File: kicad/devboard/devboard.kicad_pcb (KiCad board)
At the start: 2 copper layers, 34.5 x 25 mm, 37 parts, among them J1 USB_C_Receptacle, J2 Conn_02x02_Top_Bottom, J3 Conn_01x04_Socket, Q1 BSS138, U1 LM3940, U2 CH340G, U3 STM32G030K8Tx, Y1 12 MHz, Y2 8 MHz

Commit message: niche GND prettying up
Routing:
- net GND: track 19.8 -> 14.4 mm
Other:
- board text added: "Boot"
- board text added: "Breakout v1"
- board text added: "Reset"

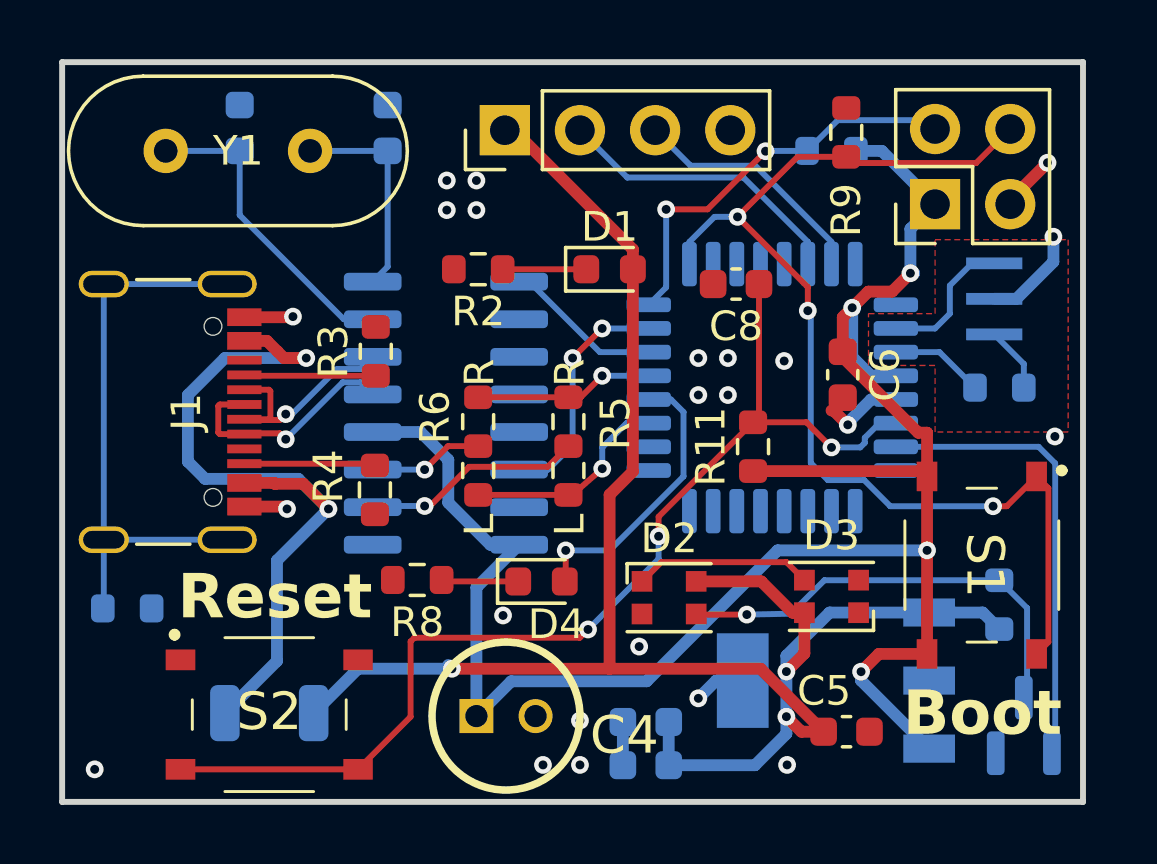
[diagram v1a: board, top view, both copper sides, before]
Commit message: Added silkscreen labels
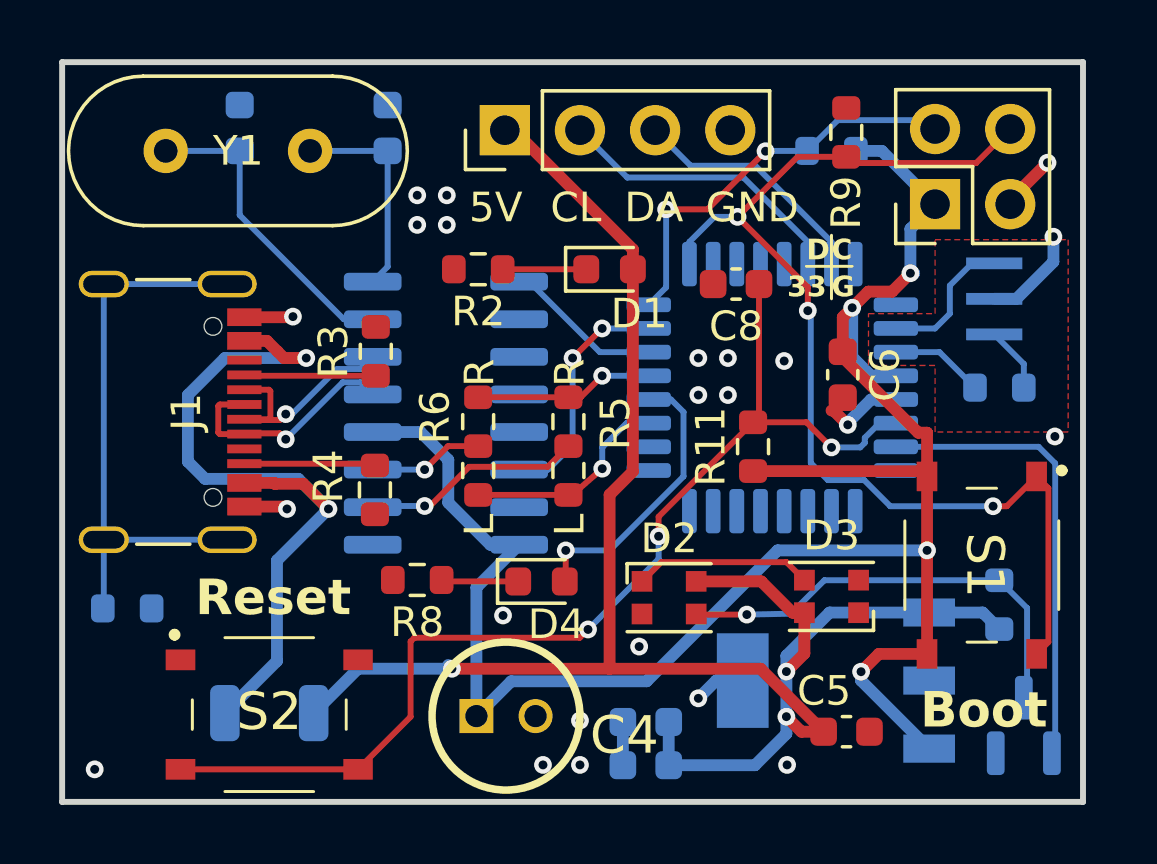
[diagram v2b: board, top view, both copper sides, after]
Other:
- board text added: "33"
- board text added: "5V"
- board text added: "C"
- board text added: "CL"
- board text added: "D"
- board text added: "DA"
- board text added: "G"
- board text added: "GND"
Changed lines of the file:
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@@
 		(tags "LED")
 		(property "Reference" "D1"
-			(at 0 -1.43 0)
+			(at 1 1.5 0)
 			(layer "F.SilkS")
 			(effects
@@
 		(tags "resistor")
 		(property "Reference" "R9"
-			(at -2.625 0 -90)
+			(at -2.375 0 -90)
 			(layer "F.SilkS")
 			(effects
@@
 		(layer "B.SilkS")
 	)
+	(gr_line
+		(start 126.15 55.9)
+		(end 127.7 55.9)
+		(stroke
+			(width 0.1)
+			(type default)
+		)
+		(layer "F.SilkS")
+	)
+	(gr_line
+		(start 127 54.85)
+		(end 127 57)
+		(stroke
+			(width 0.1)
+			(type default)
+		)
+		(layer "F.SilkS")
+	)
 	(gr_rect
 		(start 101 49)
@@
 		)
 	)
+	(gr_text "CL"
+		(at 117.5 54.5 0)
+		(layer "F.SilkS")
+		(effects
+			(font
+				(size 1 1)
+				(thickness 0.15)
+			)
+			(justify left bottom)
+		)
+	)
+	(gr_text "D"
+		(at 126.15 55.75 0)
+		(layer "F.SilkS")
+		(effects
+			(font
+				(size 0.7 0.7)
+				(thickness 0.15)
+				(bold yes)
+			)
+			(justify left bottom)
+		)
+	)
+	(gr_text "5V"
+		(at 114.75 54.5 0)
+		(layer "F.SilkS")
+		(effects
+			(font
+				(size 1 1)
+				(thickness 0.15)
+			)
+			(justify left bottom)
+		)
+	)
+	(gr_text "C"
+		(at 127 55.75 0)
+		(layer "F.SilkS")
+		(effects
+			(font
+				(size 0.7 0.7)
+				(thickness 0.15)
+				(bold yes)
+			)
+			(justify left bottom)
+		)
+	)
+	(gr_text "G"
+		(at 127 57 0)
+		(layer "F.SilkS")
+		(effects
+			(font
+				(size 0.7 0.7)
+				(thickness 0.15)
+				(bold yes)
+			)
+			(justify left bottom)
+		)
+	)
+	(gr_text "33"
+		(at 125.5 57 0)
+		(layer "F.SilkS")
+		(effects
+			(font
+				(size 0.7 0.7)
+				(thickness 0.15)
+				(bold yes)
+			)
+			(justify left bottom)
+		)
+	)
 	(gr_text "Reset"
-		(at 104.902 67.945 0)
+		(at 105.5 67.8 0)
 		(layer "F.SilkS")
 		(effects
 			(font
-				(size 1.5 1.5)
-				(thickness 0.3)
+				(size 1.2 1.2)
+				(thickness 0.25)
 				(bold yes)
 			)
@@
 	)
 	(gr_text "Boot"
-		(at 129.413 71.882 0)
+		(at 130 71.6 0)
 		(layer "F.SilkS")
 		(effects
 			(font
-				(size 1.5 1.5)
-				(thickness 0.3)
+				(size 1.2 1.2)
+				(thickness 0.25)
 				(bold yes)
 			)
@@
 		)
 	)
+	(gr_text "GND"
+		(at 122.75 54.5 0)
+		(layer "F.SilkS")
+		(effects
+			(font
+				(size 1 1)
+				(thickness 0.15)
+			)
+			(justify left bottom)
+		)
+	)
+	(gr_text "DA"
+		(at 120 54.5 0)
+		(layer "F.SilkS")
+		(effects
+			(font
+				(size 1 1)
+				(thickness 0.15)
+			)
+			(justify left bottom)
+		)
+	)
 	(gr_text "All LEDs, switches (includes R5/6), and through components go on F. Cu"
 		(at 145.796 57.912 0)
@@
 	)
 	(via
-		(at 114 54)
+		(at 113 54.5)
 		(size 0.6)
 		(drill 0.3)
@@
 	)
 	(via
-		(at 115 54)
+		(at 114 54.5)
 		(size 0.6)
 		(drill 0.3)
@@
 	)
 	(via
-		(at 115 53)
+		(at 114 53.5)
 		(size 0.6)
 		(drill 0.3)
@@
 	)
 	(via
-		(at 114 53)
+		(at 113 53.5)
 		(size 0.6)
 		(drill 0.3)

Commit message: final fixes
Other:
- board text removed: "Breakout v1"
